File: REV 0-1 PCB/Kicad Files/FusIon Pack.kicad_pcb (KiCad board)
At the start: 4 copper layers, 162 x 154 mm, 453 parts, among them J1 USB_BOARD, J2 Conn_01x05_Male, J3 B4B-XH-A(LF)(SN), J4 Conn_01x05_Male, J5 XT60, Q1 RUC002N05HZGT116, Q10 RUC002N05HZGT116, Q11 IPD60N10S4L-12, Q12 RUC002N05HZGT116, Q13 RUC002N05HZGT116, Q14 RUC002N05HZGT116, Q15 RUC002N05HZGT116, Q16 FQT5P10TF, Q17 RUC002N05HZGT116, Q18 RUC002N05HZGT116, Q19 DMPH6050SK3, Q2 RUC002N05HZGT116, Q20 IPD60N10S4L-12, Q21 RUC002N05HZGT116, Q22 DMPH6050SK3, Q23 DMPH6050SK3, Q24 IPD60N10S4L-12, Q25 IPD60N10S4L-12, Q26 IPD60N10S4L-12, Q27 IPD60N10S4L-12, Q28 IPD60N10S4L-12, Q29 IPD60N10S4L-12, Q3 RUC002N05HZGT116, Q30 IPD60N10S4L-12, Q31 IPD60N10S4L-12, Q32 IPD60N10S4L-12, Q33 IPD60N10S4L-12, Q34 FQT5P10TF, Q4 RUC002N05HZGT116, Q5 RUC002N05HZGT116, Q6 RUC002N05HZGT116, Q7 RUC002N05HZGT116, Q8 RUC002N05HZGT116, Q9 RUC002N05HZGT116, SW1 SW_Push, U1 BQ76930, U10 BQ76200, U2 STM32F072RBTx, U3 L7805, U4 AP2114H-3.3TRG1, U5 ATA6561, U6 W25Q16JVSSIQ, U7 ZXCT108x, U8 LTC3783, U9 ZXCT108x

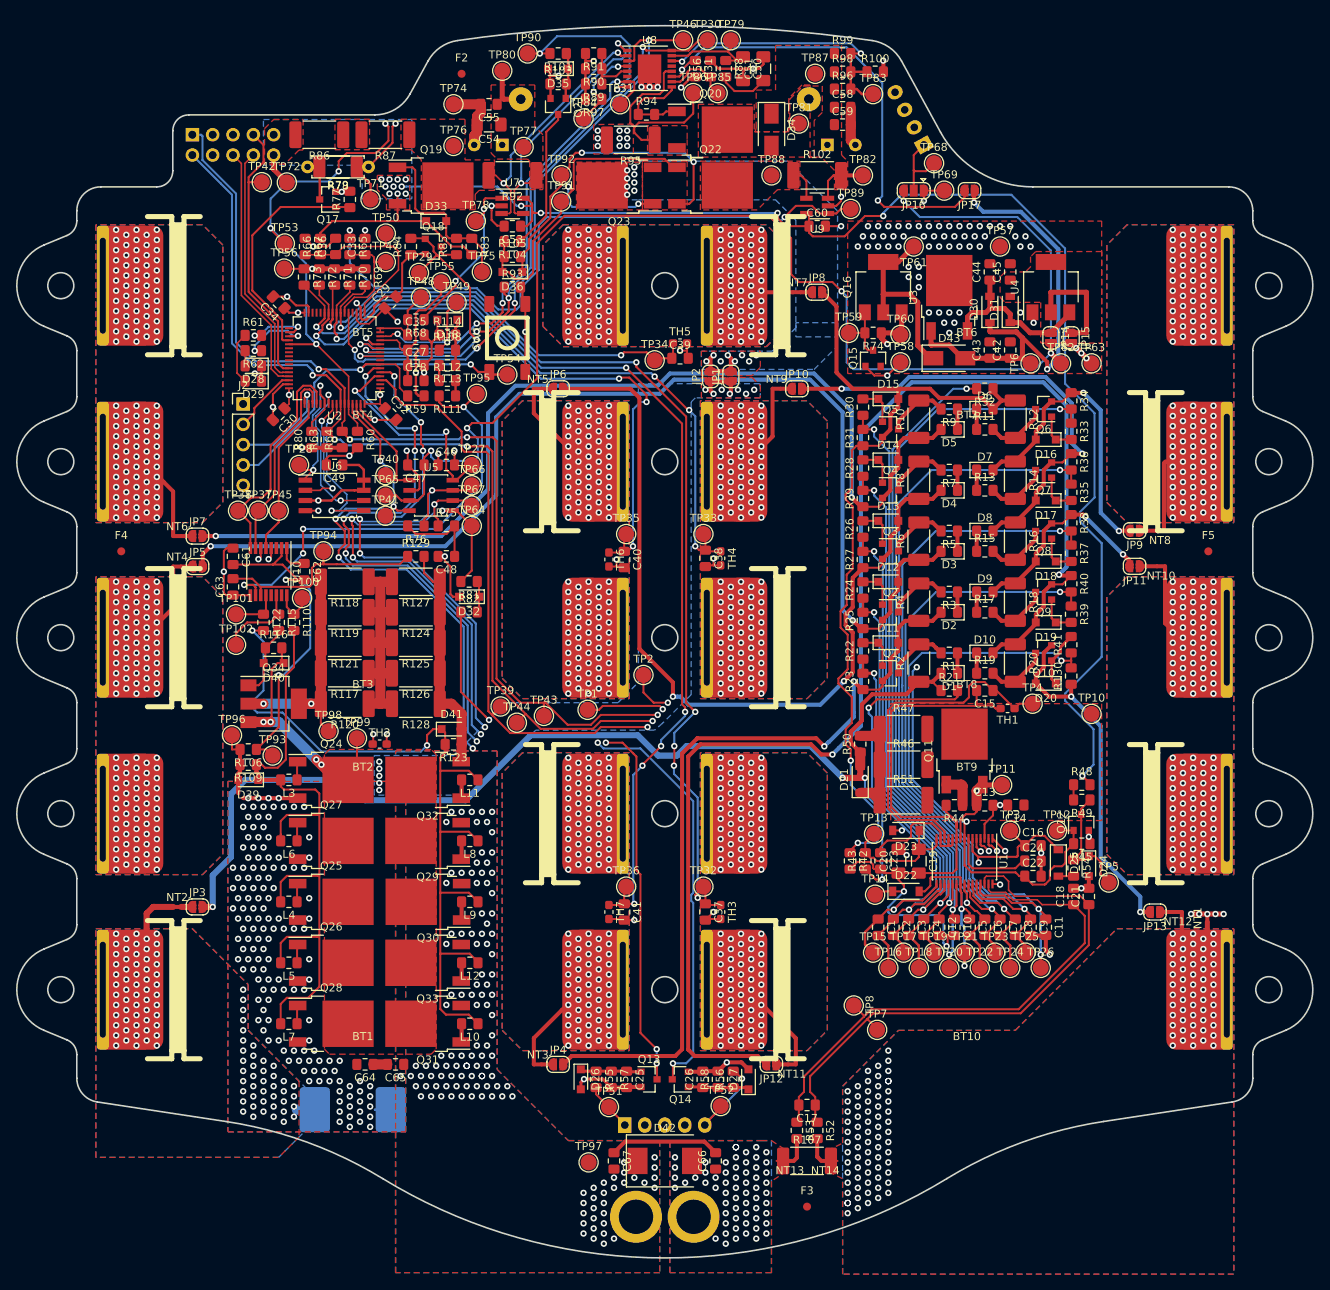
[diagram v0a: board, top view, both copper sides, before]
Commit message: Pushing regulator and interface sub-boards for FlatPack
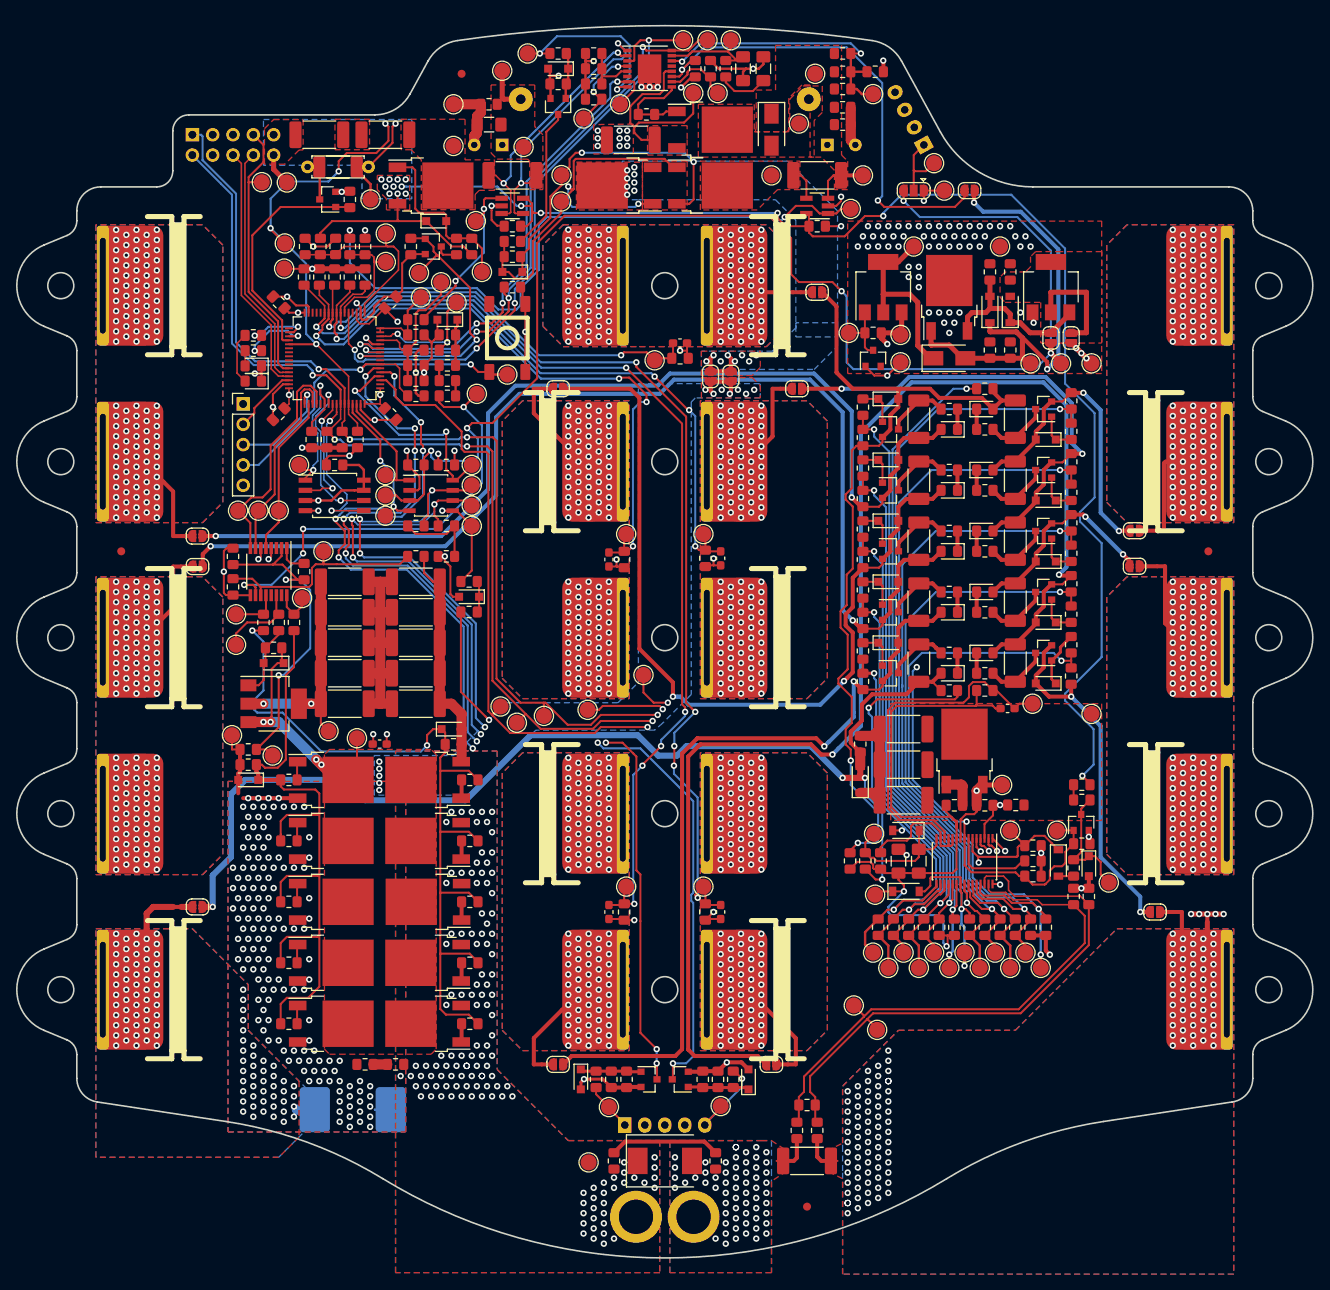
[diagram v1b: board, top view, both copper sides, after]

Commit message: Fixing working tree, pushing a bunch of SubBoards and FlatPack BOM
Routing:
- net GNDS: track 230.0 -> 230.5 mm
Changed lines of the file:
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@@
-(kicad_pcb (version 20171130) (host pcbnew "(5.1.2-1)-1")
+(kicad_pcb (version 20171130) (host pcbnew "(5.1.2)-2")
   (general
     (thickness 1.6)
     (drawings 99)
-    (tracks 4755)
+    (tracks 4756)
     (zones 0)
     (modules 453)
@@
   (segment (start 180.802 135.544) (end 179.913 135.544) (width 0.635) (layer F.Cu) (net 22))
   (segment (start 179.913 135.544) (end 179.785998 135.544) (width 0.635) (layer F.Cu) (net 22))
+  (segment (start 115.905 65.1225) (end 115.905 65.688185) (width 0.254) (layer In2.Cu) (net 22))
   (segment (start 138.765 73.205) (end 138.765 74.965) (width 0.254) (layer F.Cu) (net 23) (status 30))
   (via (at 140.162 74.965) (size 0.8) (drill 0.4) (layers F.Cu B.Cu) (net 23))
